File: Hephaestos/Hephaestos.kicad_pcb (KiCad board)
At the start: 4 copper layers, 106.8 x 61 mm, 161 parts, among them J1 Conn_01x04, J10 Conn_01x02, J11 Conn_01x02, J2 Conn_01x02, J3 Conn_01x02, J4 Conn_02x05_Counter_Clockwise, J5 Conn_01x02, J6 Conn_01x02, J7 Conn_01x02, J8 Conn_01x02, J9 Conn_01x02, Q1 CSD17577Q5A, Q2 CSD17577Q5A, U1 MCP6001-OT, U10 AP2205K-3.3, U11 MCP6001-OT, U12 MCP6001-OT, U13 MCP6001-OT, U2 MCP2542FDxMF, U3 AP2205K-5.0, U4 MCP6001-OT, U5 MCP2517FD-xSL, U6 MCP6001-OT, U7 STM32F030C8Tx, U8 MCP6001-OT, U9 MCP6001-OT, Y1 40 MHz 9 pF, Y2 16 MHz 9 pF

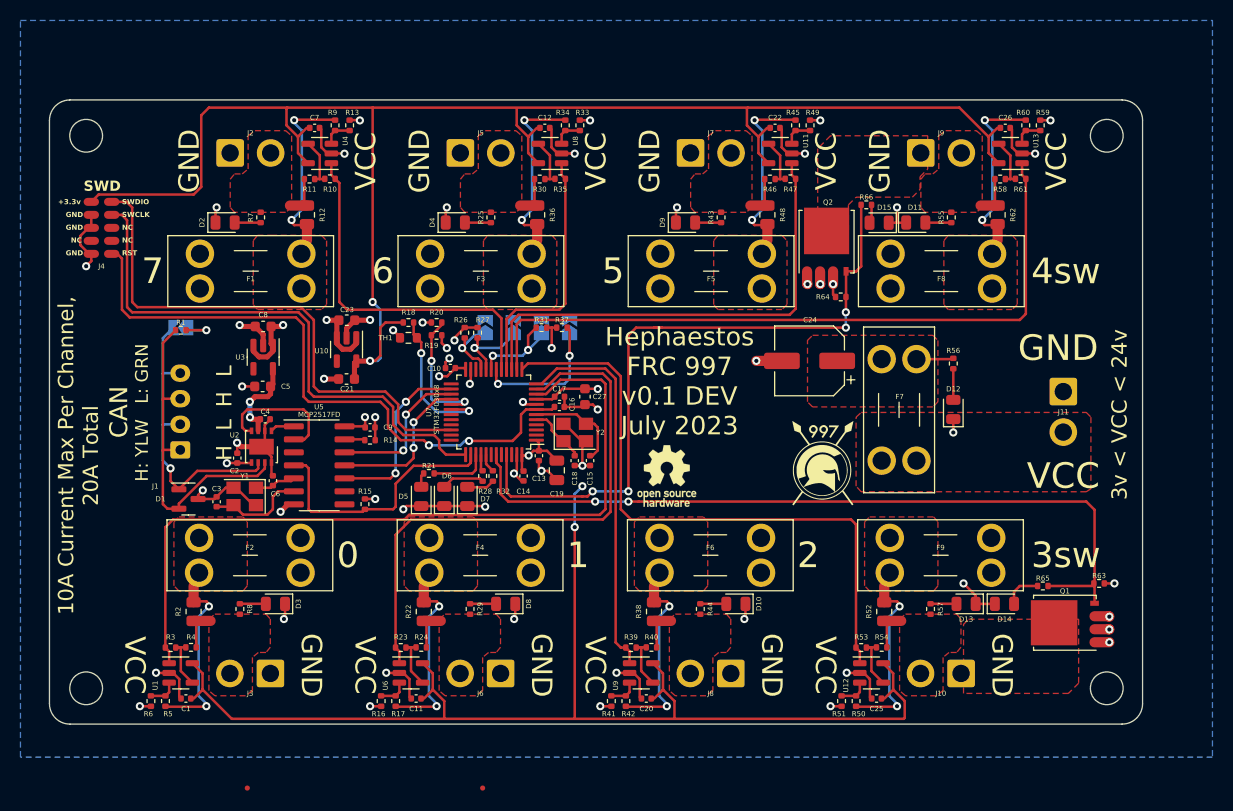
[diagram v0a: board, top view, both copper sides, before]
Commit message: Downgrade CAN controller to 2.0B for driver compatibility
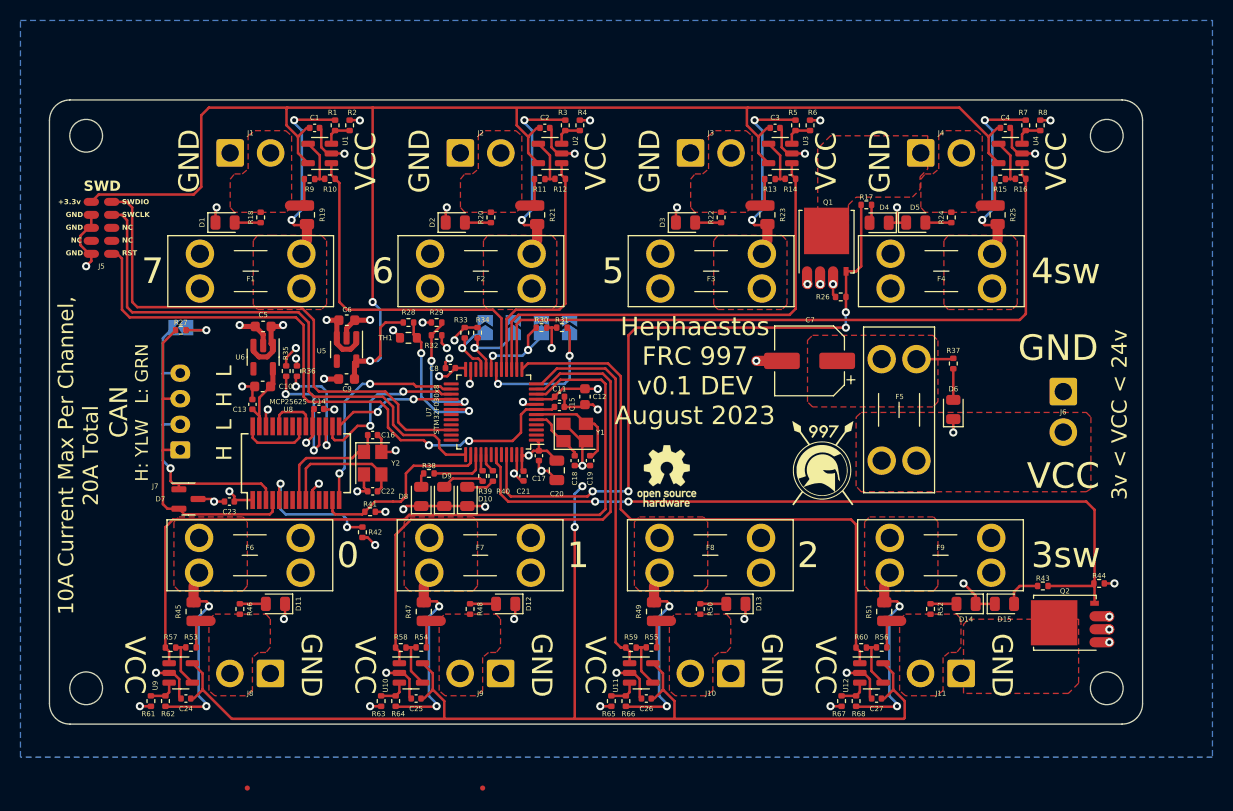
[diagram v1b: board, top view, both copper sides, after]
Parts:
- removed the U2 at (154.1, 100.9)
- removed the U5 at (159.8, 102.7)
- added R35: 1k, Resistor_SMD:R_0402_1005Metric, F.Cu at (156.6, 93.5)
- added R42: 1k, Resistor_SMD:R_0402_1005Metric, F.Cu at (164.0, 109.2)
- added U8: MCP25625-x-SS, Package_SO:SSOP-28_5.3x10.2mm_P0.65mm, F.Cu at (157.5, 102.5)
- moved C23 15.5 mm to (151.0, 106.2), turned to 180 degrees
- moved C22 15.3 mm to (165.0, 105.2), turned to 180 degrees
- moved Y2 12.9 mm to (165.0, 102.5), turned to -90 degrees
- moved C16 10.7 mm to (165.0, 99.8), turned to 180 degrees
- moved R36 9.83 mm to (157.6, 93.5), turned to -90 degrees
- moved C13 5.45 mm to (153.2, 96.8)
- moved C14 5.34 mm to (159.8, 97.2), turned to 0 degrees
- moved R41 0.90 mm to (164.8, 107.2), turned to 180 degrees
- renumbered C7 to C1, C5 to C10, C17 to C11, C27 to C12, C2 to C13, C4 to C14, C16 to C15, C6 to C16, C13 to C17, C15 to C19, C12 to C2, C19 to C20, C14 to C21, C3 to C22, C9 to C23, C1 to C24, C11 to C25, C20 to C26, C25 to C27, C22 to C3, C26 to C4, C8 to C5, C23 to C6, C24 to C7, C10 to C8, C21 to C9, D2 to D1, D7 to D10, D3 to D11, D8 to D12, D10 to D13, D13 to D14, D14 to D15, D4 to D2, D9 to D3, D15 to D4, D11 to D5, D12 to D6, D1 to D7, D5 to D8, D6 to D9, F3 to F2, F5 to F3, F8 to F4, F7 to F5, F2 to F6, F4 to F7, F6 to F8, J2 to J1, J8 to J10, J10 to J11, J5 to J2, J7 to J3, J9 to J4, J4 to J5, J11 to J6, J1 to J7, J3 to J8, J6 to J9, Q2 to Q1, Q1 to Q2, R9 to R1, R30 to R11, R35 to R12, R46 to R13, R47 to R14, R58 to R15, R61 to R16, R66 to R17, R7 to R18, R12 to R19, R13 to R2, R25 to R20, R36 to R21, R43 to R22, R48 to R23, R55 to R24, R62 to R25, R64 to R26, R1 to R27, R18 to R28, R20 to R29, R34 to R3, R31 to R30, R37 to R31, R19 to R32, R26 to R33, R27 to R34, R14 to R36, R56 to R37, R21 to R38, R28 to R39, R33 to R4, R32 to R40, R15 to R41, R65 to R43, R63 to R44, R2 to R45, R8 to R46, R22 to R47, R29 to R48, R38 to R49, R45 to R5, R44 to R50, R52 to R51, R57 to R52, R4 to R53, R24 to R54, R40 to R55, R54 to R56, R3 to R57, R23 to R58, R39 to R59, R49 to R6, R53 to R60, R6 to R61, R5 to R62, R16 to R63, R17 to R64, R41 to R65, R42 to R66, R51 to R67, R50 to R68, R60 to R7, R59 to R8, R11 to R9, U4 to U1, U6 to U10, U9 to U11, U8 to U2, U11 to U3, U13 to U4, U10 to U5, U3 to U6, U1 to U9, Y2 to Y1, Y1 to Y2
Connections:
- C13 pad 1: +3.3V -> +5V
- C14 pad 1: GND -> +3.3V
- C14 pad 2: +5V -> GND
- R36 pad 2: CAN_CS -> /CAN_CS
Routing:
- net /CAN_STBY: track 0.00 -> 13.3 mm, vias 0 -> 2
- net /RXCAN: track 12.8 -> 0.00 mm
- net /CAN_RST: track 0.00 -> 12.4 mm, vias 0 -> 2
- net /CAN_CS: track 0.00 -> 11.4 mm, vias 0 -> 2
- net /CAN_CLK_A: track 4.08 -> 12.1 mm
- net Net-(U8-RXD): track 0.00 -> 7.19 mm
- net CAN_INT: track 25.6 -> 19.0 mm
- net Net-(U8-TXD): track 0.00 -> 5.06 mm
- net CAN_SCK: track 17.5 -> 21.2 mm
- net +3.3V: track 307.0 -> 310.5 mm, vias 12 -> 13
- net /CAN_CLK_B: track 9.50 -> 12.9 mm
- net CAN_PICO: track 15.2 -> 12.2 mm
- net GND: track 137.7 -> 134.9 mm, vias 53 -> 57
- net /TXCAN: track 2.37 -> 0.00 mm
- net CAN_CS: track 1.90 -> 0.00 mm
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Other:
- board text added: "Hephaestos FRC 997 v0.1 DEV August 2023"
- board text added: "MCP25625"
- board text removed: "Hephaestos FRC 997 v0.1 DEV July 2023"
- board text removed: "MCP2517FD"

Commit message: Switch to F042 w/ internal CAN controller, change stackup
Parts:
- removed C10: 2.2 uF, Capacitor_SMD:C_0603_1608Metric
- removed C13, C14, C23: 0.1 uF, Capacitor_SMD:C_0402_1005Metric
- removed C16, C22: 10 pF, Capacitor_SMD:C_0402_1005Metric
- removed R35, R36, R41, R42: 1k, Resistor_SMD:R_0402_1005Metric
- removed U6: AP2205K-5.0, Package_TO_SOT_SMD:SOT-23-5
- removed U7: STM32F030C8Tx, Package_QFP:LQFP-48_7x7mm_P0.5mm
- removed Y2: 40 MHz 9 pF, Crystal:Crystal_SMD_3225-4Pin_3.2x2.5mm
- added C28: 0.1 uF, Capacitor_SMD:C_0402_1005Metric, F.Cu at (171.0, 100.8)
- added R69: 1k, Resistor_SMD:R_0402_1005Metric, F.Cu at (236.2, 114.5)
- added R70: 1k, Resistor_SMD:R_0402_1005Metric, F.Cu at (210.2, 86.2)
- added R71: 1k, Resistor_SMD:R_0402_1005Metric, F.Cu at (168.2, 102.5)
- added U13: STM32F042C6Tx, Package_QFP:LQFP-48_7x7mm_P0.5mm, F.Cu at (176.8, 97.6)
- C5: value 1 uF 35v -> 0.1 uF; footprint Capacitor_SMD:C_0603_1608Metric -> Capacitor_SMD:C_0402_1005Metric
- U8: value MCP25625-x-SS -> SN65HVD232; footprint Package_SO:SSOP-28_5.3x10.2mm_P0.65mm -> Package_SO:SOIC-8_3.9x4.9mm_P1.27mm
- moved C5 18.0 mm to (163.2, 104.8), turned to 90 degrees
- moved U8 2.57 mm to (158.8, 104.8), turned to 180 degrees
- moved R44 2.26 mm to (233.8, 114.0), turned to 90 degrees
- moved R26 1.95 mm to (209.2, 87.5)
- moved R39 0.25 mm to (175.8, 104.0)
- moved R40 0.25 mm to (176.8, 104.0)
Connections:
- net /channel0/H renamed Net-(F6-Pad1)
- net /channel1/H renamed Net-(F7-Pad1)
- net /channel2/H renamed Net-(F8-Pad1)
- net /channel3/H renamed Net-(F9-Pad1)
- net /channel4/H renamed Net-(F4-Pad1)
- net /channel5/H renamed Net-(F3-Pad1)
- net /channel6/H renamed Net-(F2-Pad1)
- net /channel7/H renamed Net-(F1-Pad1)
- C5 pad 1: VCC -> GND
- C5 pad 2: GND -> +3.3V
- Q1 pad 4: SW4 -> Net-(Q1-G)
- Q2 pad 4: SW3 -> Net-(Q2-G)
- U8 pad 1: +3.3V -> CAN_TX
- U8 pad 2: unconnected-(U8-NC-Pad2) -> GND
- U8 pad 3: CANL -> +3.3V
- U8 pad 4: CANH -> CAN_RX
- U8 pad 5: /CAN_STBY -> unconnected-(U8-NC-Pad5)
- U8 pad 6: unconnected-(U8-~{Tx1RTS}-Pad6) -> CANL
- U8 pad 7: unconnected-(U8-~{Tx2RTS}-Pad7) -> CANH
- U8 pad 8: /CAN_CLK_A -> unconnected-(U8-NC-Pad8)
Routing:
- net CAN_SCK: track 21.2 -> 0.00 mm, vias 2 -> 0
- net CAN_TX: track 0.00 -> 19.1 mm, vias 0 -> 2
- net CAN_INT: track 19.0 -> 0.00 mm
- net CAN_POCI: track 16.3 -> 0.00 mm, vias 2 -> 0
- net CAN_RX: track 0.00 -> 16.0 mm, vias 0 -> 2
- net /CAN_STBY: track 13.3 -> 0.00 mm, vias 2 -> 0
- net /CAN_CLK_B: track 12.9 -> 0.00 mm
- net /CAN_RST: track 12.4 -> 0.00 mm, vias 2 -> 0
- net CAN_PICO: track 12.2 -> 0.00 mm, vias 2 -> 0
- net /CAN_CLK_A: track 12.1 -> 0.00 mm
- net /CAN_CS: track 11.4 -> 0.00 mm, vias 2 -> 0
- net Net-(U13-PF11): track 0.00 -> 11.2 mm, vias 0 -> 2
- net +5V: track 8.12 -> 0.00 mm
- net Net-(U8-RXD): track 7.19 -> 0.00 mm
- net VCC: track 17.2 -> 10.6 mm, vias 3 -> 2
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- added copper zone on B.Cu, net +3.3V
- added copper zone on In1.Cu, net GND
- added copper zone on In2.Cu, net GND
- added copper zone on B.Cu, net VCC
- removed copper zone on In1.Cu, net +3.3V
- removed copper zone on In2.Cu, net +3.3V
- removed copper zone on B.Cu, net GND
- removed copper zone on In1.Cu, net VCC
- removed copper zone on In2.Cu, net VCC
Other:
- board text added: "STM32F042C6"
- board text removed: "MCP25625"
- board text removed: "STM32F030x8"
